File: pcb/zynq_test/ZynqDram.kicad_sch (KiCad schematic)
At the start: 1 part, among them U1 XC7Z020-2CLG400I

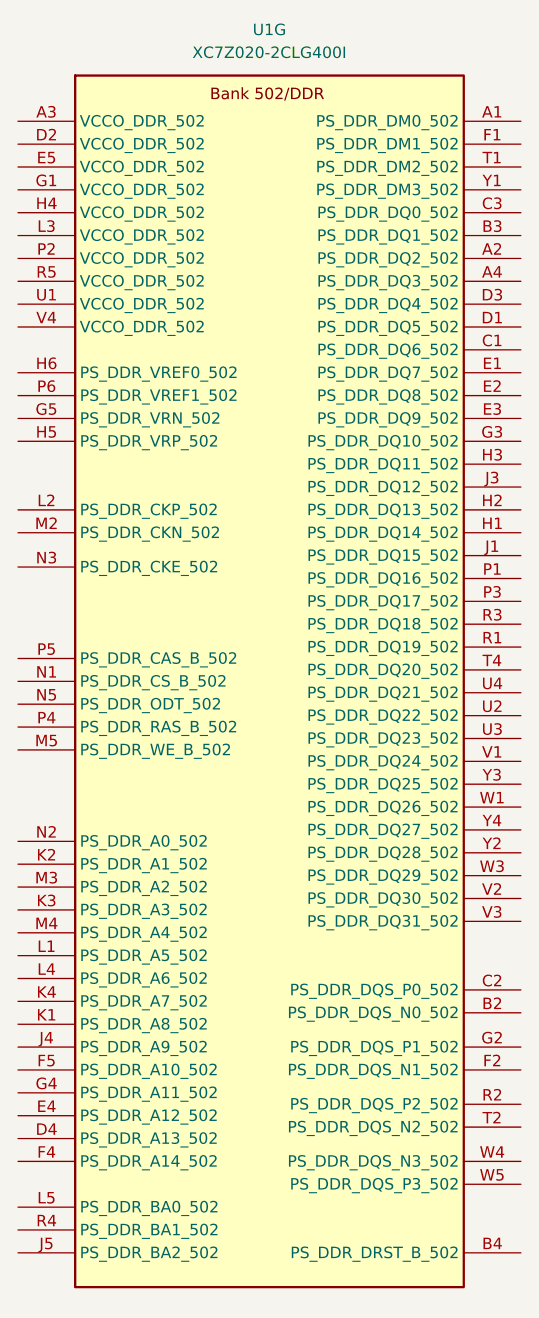
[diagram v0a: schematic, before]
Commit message: Finished PS, started on PWR
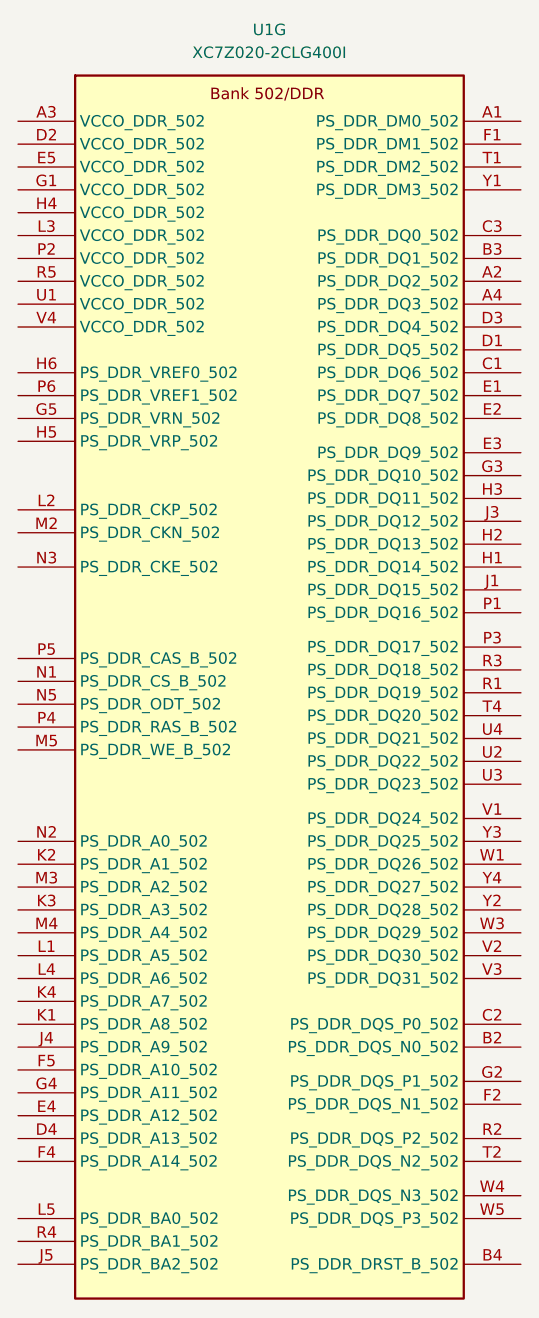
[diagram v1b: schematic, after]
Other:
- moved on the sheet: U1G

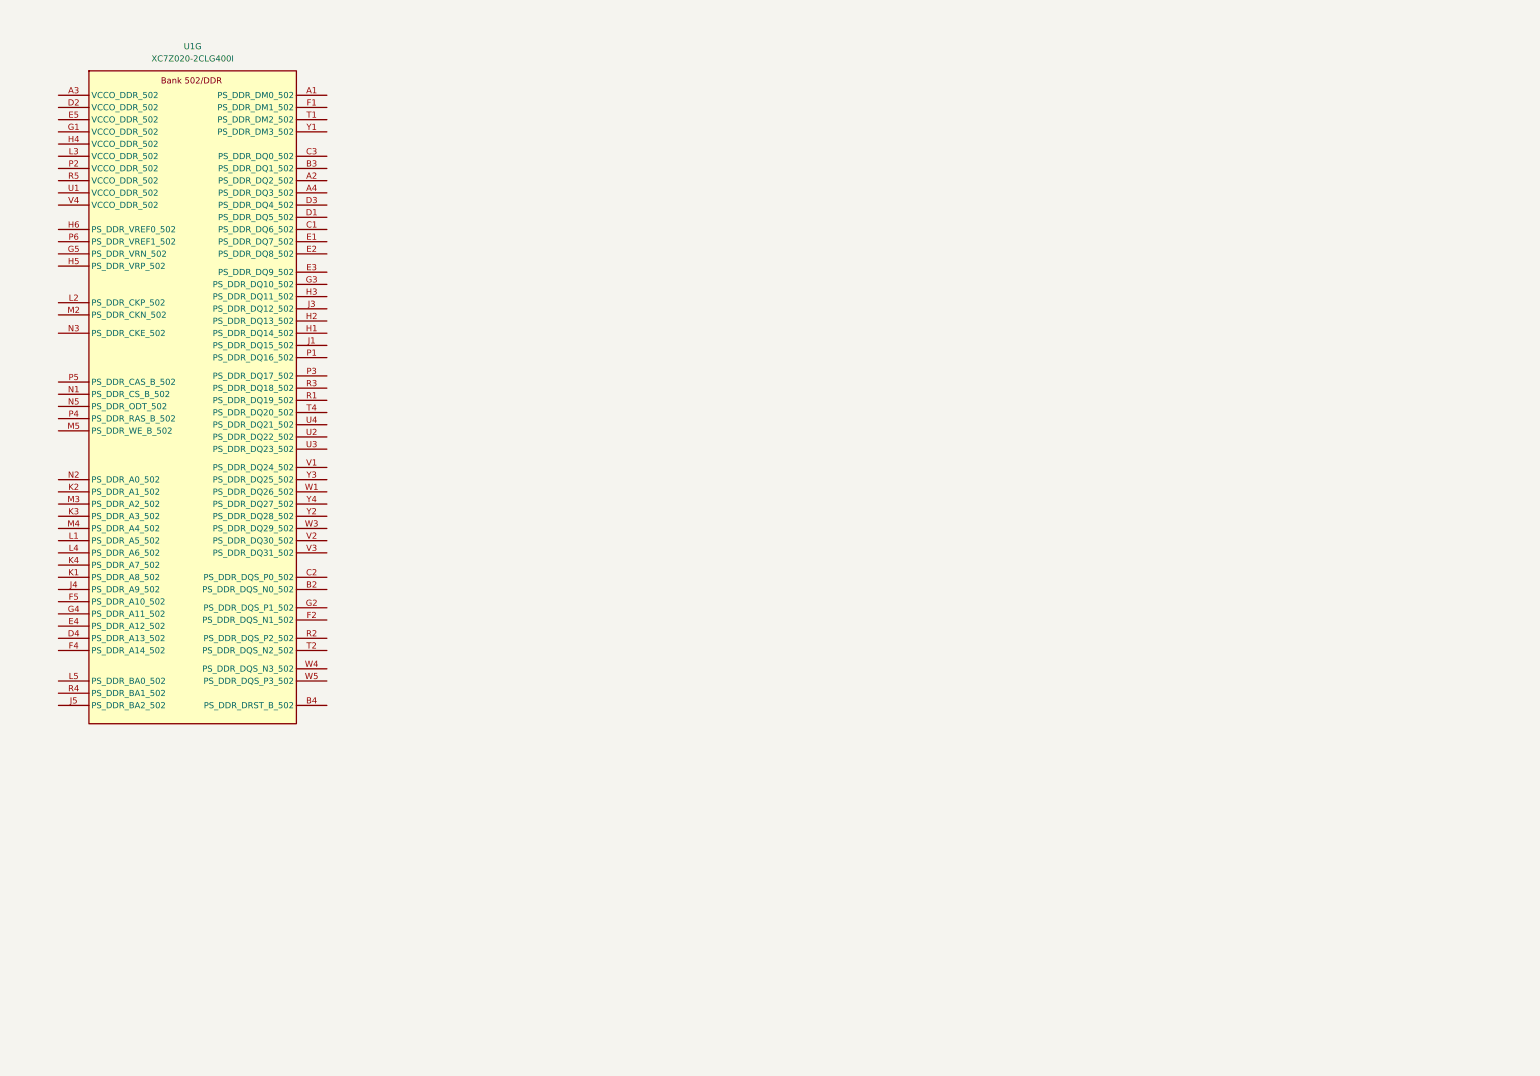
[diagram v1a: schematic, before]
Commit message: Finished FPGA decouploing, and jtag programmer
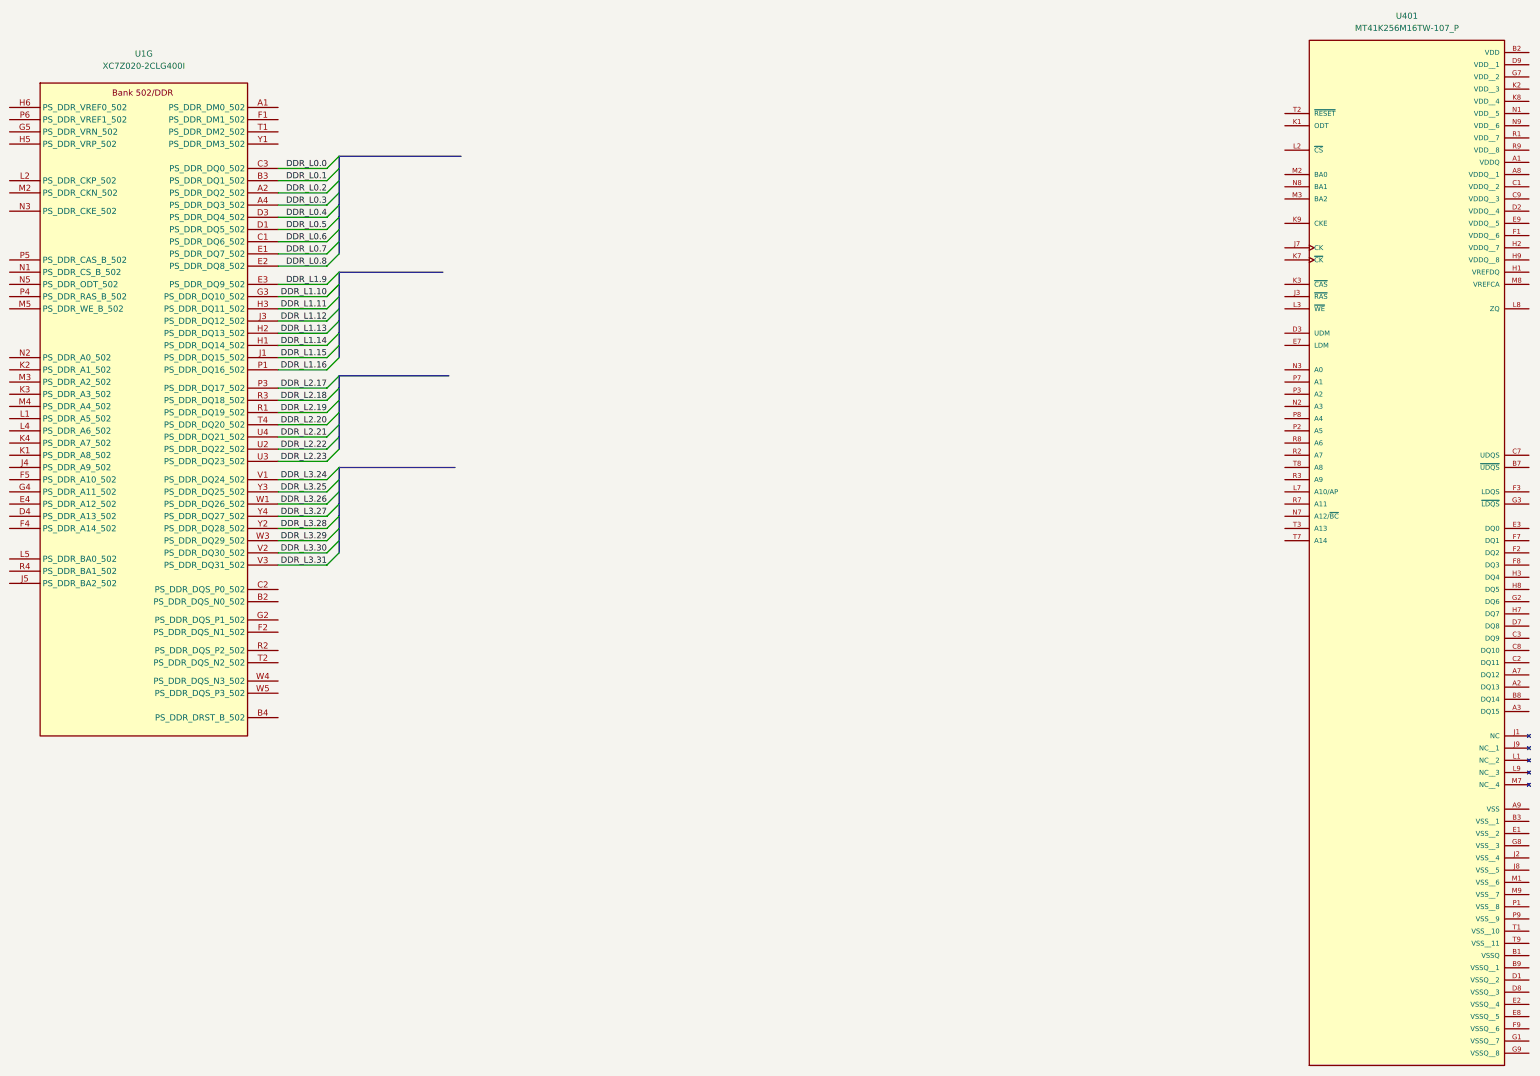
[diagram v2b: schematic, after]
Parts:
- added U401: MT41K256M16TW-107_P, MT41K256M16TW-107_P:BGA96C80P9X16_1400X800X120, symbol ddr3:MT41K256M16TW-107_P
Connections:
- net DDR_L0.2: now reaches U1.A2 (PS_DDR_DQ2_502)
- net DDR_L0.3: now reaches U1.A4 (PS_DDR_DQ3_502)
- net DDR_L0.1: now reaches U1.B3 (PS_DDR_DQ1_502)
- net DDR_L0.6: now reaches U1.C1 (PS_DDR_DQ6_502)
- net DDR_L0.0: now reaches U1.C3 (PS_DDR_DQ0_502)
- net DDR_L0.5: now reaches U1.D1 (PS_DDR_DQ5_502)
- net DDR_L0.4: now reaches U1.D3 (PS_DDR_DQ4_502)
- net DDR_L0.7: now reaches U1.E1 (PS_DDR_DQ7_502)
- net DDR_L0.8: now reaches U1.E2 (PS_DDR_DQ8_502)
- net DDR_L1.9: now reaches U1.E3 (PS_DDR_DQ9_502)
- net DDR_L1.10: now reaches U1.G3 (PS_DDR_DQ10_502)
- net DDR_L1.14: now reaches U1.H1 (PS_DDR_DQ14_502)
- net DDR_L1.13: now reaches U1.H2 (PS_DDR_DQ13_502)
- net DDR_L1.11: now reaches U1.H3 (PS_DDR_DQ11_502)
- net DDR_L1.15: now reaches U1.J1 (PS_DDR_DQ15_502)
- net DDR_L1.12: now reaches U1.J3 (PS_DDR_DQ12_502)
- net DDR_L1.16: now reaches U1.P1 (PS_DDR_DQ16_502)
- net DDR_L2.17: now reaches U1.P3 (PS_DDR_DQ17_502)
- net DDR_L2.19: now reaches U1.R1 (PS_DDR_DQ19_502)
- net DDR_L2.18: now reaches U1.R3 (PS_DDR_DQ18_502)
- net DDR_L2.20: now reaches U1.T4 (PS_DDR_DQ20_502)
- net DDR_L2.22: now reaches U1.U2 (PS_DDR_DQ22_502)
- net DDR_L2.23: now reaches U1.U3 (PS_DDR_DQ23_502)
- net DDR_L2.21: now reaches U1.U4 (PS_DDR_DQ21_502)
- net DDR_L3.24: now reaches U1.V1 (PS_DDR_DQ24_502)
- net DDR_L3.30: now reaches U1.V2 (PS_DDR_DQ30_502)
- net DDR_L3.31: now reaches U1.V3 (PS_DDR_DQ31_502)
- net DDR_L3.26: now reaches U1.W1 (PS_DDR_DQ26_502)
- net DDR_L3.29: now reaches U1.W3 (PS_DDR_DQ29_502)
- net DDR_L3.28: now reaches U1.Y2 (PS_DDR_DQ28_502)
- net DDR_L3.25: now reaches U1.Y3 (PS_DDR_DQ25_502)
- net DDR_L3.27: now reaches U1.Y4 (PS_DDR_DQ27_502)

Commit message: Finished boot media, added structure for IO
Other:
- moved on the sheet: U1G, U401

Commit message: Finished HDMI
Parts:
- U1: footprint Zynq:CLG400_ZYNQ-7000_AMD -> Package_BGA:Xilinx_CLG400
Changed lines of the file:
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@@
 			)
 		)
-		(property "Footprint" "Zynq:CLG400_ZYNQ-7000_AMD"
+		(property "Footprint" "Package_BGA:Xilinx_CLG400"
 			(at 38.1 7.62 0)
 			(effects

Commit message: Started on DDR3
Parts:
- removed U401: MT41K256M16TW-107_P, MT41K256M16TW-107_P:BGA96C80P9X16_1400X800X120, symbol ddr3:MT41K256M16TW-107_P
- added U401, U402: MT41K256M16TW-107, dram:BGA96C80P9X16_1400X800X120, symbol ddr3:MT41K256M16TW-107
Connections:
- net DDR_L0.DM: now reaches U1.A1 (PS_DDR_DM0_502)
- net DDR_L0.DQS_N: now reaches U1.B2 (PS_DDR_DQS_N0_502)
- net DDR_CTR.RST: now reaches U1.B4 (PS_DDR_DRST_B_502)
- net DDR_CTR.RST: now also U401.T2 (~{RESET}), U402.T2 (~{RESET})
- net DDR_L0.DQS_P: now reaches U1.C2 (PS_DDR_DQS_P0_502)
- net DDR_ADDR13: now reaches U1.D4 (PS_DDR_A13_502)
- net DDR_ADDR13: now also U401.T3 (A13), U402.T3 (A13)
- net DDR_ADDR12: now reaches U1.E4 (PS_DDR_A12_502)
- net DDR_ADDR12: now also U401.N7 (A12/~{BC}), U402.N7 (A12/~{BC})
- net DDR_L1.DM: now reaches U1.F1 (PS_DDR_DM1_502)
- net DDR_L1.DQS_N: now reaches U1.F2 (PS_DDR_DQS_N1_502)
- net DDR_ADDR14: now reaches U1.F4 (PS_DDR_A14_502)
- net DDR_ADDR14: now also U401.T7 (A14), U402.T7 (A14)
- net DDR_ADDR10: now reaches U1.F5 (PS_DDR_A10_502)
- net DDR_ADDR10: now also U401.L7 (A10/AP), U402.L7 (A10/AP)
- net DDR_L1.DQS_P: now reaches U1.G2 (PS_DDR_DQS_P1_502)
- net DDR_ADDR11: now reaches U1.G4 (PS_DDR_A11_502)
- net DDR_ADDR11: now also U401.R7 (A11), U402.R7 (A11)
- net DDR_ADDR9: now reaches U1.J4 (PS_DDR_A9_502)
- net DDR_ADDR9: now also U401.R3 (A9), U402.R3 (A9)
- net DDR_CTR.BA2: now reaches U1.J5 (PS_DDR_BA2_502)
- net DDR_CTR.BA2: now also U401.M3 (BA2), U402.M3 (BA2)
- net DDR_ADDR8: now reaches U1.K1 (PS_DDR_A8_502)
- net DDR_ADDR8: now also U401.T8 (A8), U402.T8 (A8)
- net DDR_ADDR1: now reaches U1.K2 (PS_DDR_A1_502)
- net DDR_ADDR1: now also U401.P7 (A1), U402.P7 (A1)
- net DDR_ADDR3: now reaches U1.K3 (PS_DDR_A3_502)
- net DDR_ADDR3: now also U401.N2 (A3), U402.N2 (A3)
- net DDR_ADDR7: now reaches U1.K4 (PS_DDR_A7_502)
- net DDR_ADDR7: now also U401.R2 (A7), U402.R2 (A7)
- net DDR_ADDR5: now reaches U1.L1 (PS_DDR_A5_502)
- net DDR_ADDR5: now also U401.P2 (A5), U402.P2 (A5)
- net DDR_CTR.CLK_P: now reaches U1.L2 (PS_DDR_CKP_502)
- net DDR_CTR.CLK_P: now also U401.J7 (CK), U402.J7 (CK)
- net DDR_ADDR6: now reaches U1.L4 (PS_DDR_A6_502)
- net DDR_ADDR6: now also U401.R8 (A6), U402.R8 (A6)
- net DDR_CTR.BA0: now reaches U1.L5 (PS_DDR_BA0_502)
- net DDR_CTR.BA0: now also U401.M2 (BA0), U402.M2 (BA0)
- net DDR_CTR.CLK_N: now reaches U1.M2 (PS_DDR_CKN_502)
- net DDR_CTR.CLK_N: now also U401.K7 (~{CK}), U402.K7 (~{CK})
- net DDR_ADDR2: now reaches U1.M3 (PS_DDR_A2_502)
- net DDR_ADDR2: now also U401.P3 (A2), U402.P3 (A2)
- net DDR_ADDR4: now reaches U1.M4 (PS_DDR_A4_502)
- net DDR_ADDR4: now also U401.P8 (A4), U402.P8 (A4)
- net DDR_CTR.WE: now reaches U1.M5 (PS_DDR_WE_B_502)
- net DDR_CTR.WE: now also U401.L3 (~{WE}), U402.L3 (~{WE})
- net DDR_CTR.CS: now reaches U1.N1 (PS_DDR_CS_B_502)
- net DDR_CTR.CS: now also U401.L2 (~{CS}), U402.L2 (~{CS})
- net DDR_ADDR0: now reaches U1.N2 (PS_DDR_A0_502)
- net DDR_ADDR0: now also U401.N3 (A0), U402.N3 (A0)
- net DDR_CTR.CLK_E: now reaches U1.N3 (PS_DDR_CKE_502)
- net DDR_CTR.CLK_E: now also U401.K9 (CKE), U402.K9 (CKE)
- net DDR_CTR.ODT: now reaches U1.N5 (PS_DDR_ODT_502)
- net DDR_CTR.ODT: now also U401.K1 (ODT), U402.K1 (ODT)
- net DDR_CTR.RAS: now reaches U1.P4 (PS_DDR_RAS_B_502)
- net DDR_CTR.RAS: now also U401.J3 (~{RAS}), U402.J3 (~{RAS})
- net DDR_CTR.CAS: now reaches U1.P5 (PS_DDR_CAS_B_502)
- net DDR_CTR.CAS: now also U401.K3 (~{CAS}), U402.K3 (~{CAS})
- net DDR_L2.DQS_P: now reaches U1.R2 (PS_DDR_DQS_P2_502)
- net DDR_CTR.BA1: now reaches U1.R4 (PS_DDR_BA1_502)
- net DDR_CTR.BA1: now also U401.N8 (BA1), U402.N8 (BA1)
- net DDR_L2.DM: now reaches U1.T1 (PS_DDR_DM2_502)
- net DDR_L2.DQS_N: now reaches U1.T2 (PS_DDR_DQS_N2_502)
- net DDR_L3.DQS_P: now reaches U1.W4 (PS_DDR_DQS_N3_502)
- net DDR_L3.DQS_N: now reaches U1.W5 (PS_DDR_DQS_P3_502)
- net DDR_L3.DM: now reaches U1.Y1 (PS_DDR_DM3_502)
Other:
- moved on the sheet: U1G

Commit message: Connected DDR3, cleaned up some thing
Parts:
- removed unit 2 of U401
- removed unit 2 of U402
- added C401: 470n, symbol Device:C
- added C402, C405, C408, C412: 4u7, symbol Device:C_Small
- added C403, C406, C409, C411: 470n, symbol Device:C_Small
- added C404, C407, C410, C413, C414: 100n, symbol Device:C_Small
- added R401, R402, R406: 80R, symbol Device:R_US
- added R403: 4k7, symbol Device:R_US
- added R404, R405: 240R, symbol Device:R
- added R407, R408, R409, R410, R411, R412, R413, R414, R415, R416, R417, R418, R419, R420, R421, R422, R423, R424, R425, R426, R427: 40R, symbol Device:R_US
- renumbered U1 to U202
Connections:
- net DDR_L0.8 is gone; now on net DDR_L1.8: U202.E2 (PS_DDR_DQ8_502)
- net DDR_L1.16 is gone; now on net DDR_L2.16: U202.P1 (PS_DDR_DQ16_502)
- net DDR_ADDR0: now also R407.2
- net DDR_ADDR1: now also R409.2
- net DDR_ADDR10: now also R413.2
- net DDR_ADDR11: now also R416.2
- net DDR_ADDR12: now also R419.2
- net DDR_ADDR13: now also R422.2
- net DDR_ADDR14: now also R425.2
- net DDR_ADDR2: now also R412.2
- net DDR_ADDR3: now also R415.2
- net DDR_ADDR4: now also R418.2
- net DDR_ADDR5: now also R421.2
- net DDR_ADDR6: now also R424.2
- net DDR_ADDR7: now also R427.2
- net DDR_ADDR8: now also R408.2
- net DDR_ADDR9: now also R410.2
- net DDR_CTR.CAS: now also R414.2
- net DDR_CTR.CLK_E: now also R411.2
- net DDR_CTR.CLK_N: now also R406.2
- net DDR_CTR.CLK_P: now also R406.1
- net DDR_CTR.CS: now also R417.2
- net DDR_CTR.ODT: now also R420.2
- net DDR_CTR.RAS: now also R423.2
- net DDR_CTR.RST: now also R403.1
- net DDR_CTR.WE: now also R426.2
- net DDR_L0.0: now also U401.E3 (DQ0)
- net DDR_L0.1: now also U401.F7 (DQ1)
- net DDR_L0.2: now also U401.F2 (DQ2)
- net DDR_L0.3: now also U401.F8 (DQ3)
- net DDR_L0.4: now also U401.H3 (DQ4)
- net DDR_L0.5: now also U401.H8 (DQ5)
- net DDR_L0.6: now also U401.G2 (DQ6)
- net DDR_L0.7: now also U401.H7 (DQ7)
- net DDR_L0.DM: now also U401.E7 (LDM)
- net DDR_L0.DQS_N: now also U401.G3 (~{LDQS})
- net DDR_L0.DQS_P: now also U401.F3 (LDQS)
- net DDR_L1.10: now also U401.C8 (DQ10)
- net DDR_L1.11: now also U401.C2 (DQ11)
- net DDR_L1.12: now also U401.A7 (DQ12)
- net DDR_L1.13: now also U401.A2 (DQ13)
- net DDR_L1.14: now also U401.B8 (DQ14)
- net DDR_L1.15: now also U401.A3 (DQ15)
- net DDR_L1.9: now also U401.C3 (DQ9)
- net DDR_L1.DM: now also U401.D3 (UDM)
- net DDR_L1.DQS_N: now also U401.B7 (~{UDQS})
- net DDR_L1.DQS_P: now also U401.C7 (UDQS)
- net DDR_L2.17: now also U402.F7 (DQ1)
- net DDR_L2.18: now also U402.F2 (DQ2)
- net DDR_L2.19: now also U402.F8 (DQ3)
- net DDR_L2.20: now also U402.H3 (DQ4)
- net DDR_L2.21: now also U402.H8 (DQ5)
- net DDR_L2.22: now also U402.G2 (DQ6)
- net DDR_L2.23: now also U402.H7 (DQ7)
- net DDR_L2.DM: now also U402.E7 (LDM)
- net DDR_L2.DQS_N: now also U402.G3 (~{LDQS})
- net DDR_L2.DQS_P: now also U402.F3 (LDQS)
- net DDR_L3.24: now also U402.D7 (DQ8)
- net DDR_L3.25: now also U402.C3 (DQ9)
- net DDR_L3.26: now also U402.C8 (DQ10)
- net DDR_L3.27: now also U402.C2 (DQ11)
- net DDR_L3.28: now also U402.A7 (DQ12)
- net DDR_L3.29: now also U402.A2 (DQ13)
- net DDR_L3.30: now also U402.B8 (DQ14)
- net DDR_L3.31: now also U402.A3 (DQ15)
- net DDR_L3.DM: now also U402.D3 (UDM)
- net DDR_L3.DQS_N: now also U402.B7 (~{UDQS})
- net DDR_L3.DQS_P: now also U402.C7 (UDQS)
- net DDR_L1.8: now reaches U401.D7 (DQ8)
- net at U401.L8 (ZQ): now also R404.1
- net DDR_L2.16: now reaches U402.E3 (DQ0)
- net at U402.L8 (ZQ): now also R405.1
- net at U202.G5 (PS_DDR_VRN_502): now also R401.2
- net at U202.H5 (PS_DDR_VRP_502): now also R402.1
- net V_{TT 0.675} REF: now reaches U202.H6 (PS_DDR_VREF0_502)
- net V_{TT 0.675} REF: now also U202.P6 (PS_DDR_VREF1_502), C401.1
- new net +1V35: R401.1
- new net +V_{TT} 0V675: C402.1, C403.1, C404.1, C405.1, C406.1, C407.1, C408.1, C409.1, C410.1, C411.1, C412.1, C413.1, C414.1, R407.1, R408.1, R409.1, R410.1, R411.1, R412.1, R413.1, R414.1, R415.1, R416.1, R417.1, R418.1, R419.1, R420.1, R421.1, R422.1, R423.1, R424.1, R425.1, R426.1, R427.1
- new net GND: C401.2, C402.2, C403.2, C404.2, C405.2, C406.2, C407.2, C408.2, C409.2, C410.2, C411.2, C412.2, C413.2, C414.2, R402.2, R403.2, R404.2, R405.2
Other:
- added sheet Dram PWR (dram_pwr.kicad_sch)
- note added: "DDR Termination"
- note added: "DDR Termination Bypass Capacitors"
- note added: "Keep Termination close to last ddr3 in chain"
- note added: "Keep close to termination resistors"
- moved on the sheet: U202G, U401A, U402A

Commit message: Finished Power Supply
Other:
- title: (none) -> DDR3
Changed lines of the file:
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@@
 	(paper "A3")
 	(title_block
-		(date "2025-09-06")
-		(rev "v1.0")
+		(title "DDR3")
+		(date "2025-09-13")
+		(rev "A")
 	)
 	(bus_alias "DDR_CTR"
